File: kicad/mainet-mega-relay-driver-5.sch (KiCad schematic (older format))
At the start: 8 parts, among them J34 Screw_Terminal_01x03, K5 SANYOU_SRD_Form_C, Q5 2N3904, U6 4N37

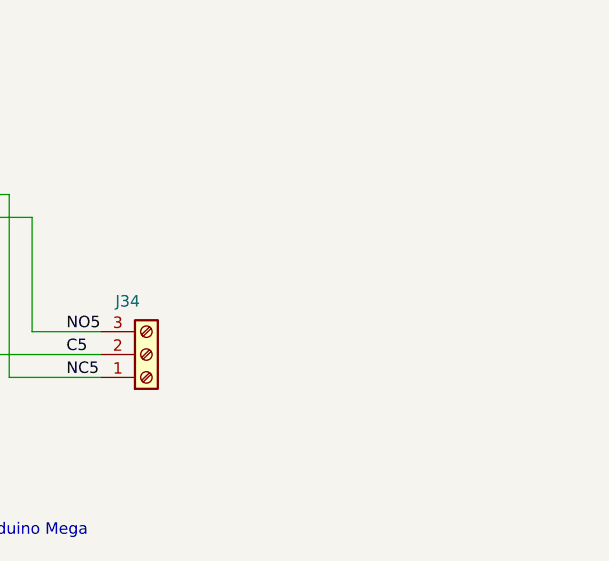
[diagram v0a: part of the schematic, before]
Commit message: KICAD: Actualizar esquemáticos
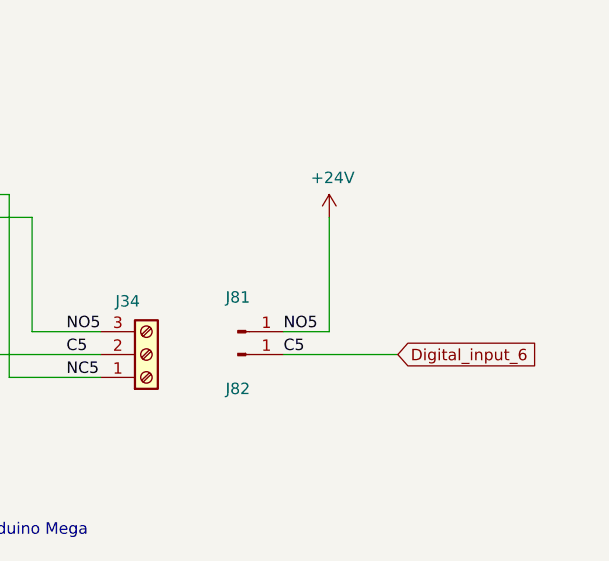
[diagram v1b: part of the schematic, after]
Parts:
- added J81, J82: Conn_01x01_Male, symbol Connector:Conn_01x01_Male
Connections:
- net C5 renamed Digital_input_6
- net Digital_input_6: now also J82.1 (Pin_1)
- net NO5 renamed +24V
- net +24V: now also J81.1 (Pin_1)
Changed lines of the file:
@@
 Sheet 11 21
 Title "Mainet-mega -- "
-Date "2021-04-06"
+Date "2021-04-07"
 Rev "1.0"
 Comp "Tovenca"
@@
 Text Notes 3650 4250 0    50   ~ 0
 D17-jogForwardControl
+$Comp
+L Connector:Conn_01x01_Male J?
+U 1 1 60704034
+P 8700 3600
+AR Path="/5FC25793/5FD90A95/60704034" Ref="J?"  Part="1"
+AR Path="/5FC25793/5FD919F3/60704034" Ref="J81"  Part="1"
+F 0 "J81" H 8700 3750 50  0000 C CNN
+F 1 "Conn_01x01_Male" H 8808 3690 50  0001 C CNN
+F 2 "" H 8700 3600 50  0001 C CNN
+F 3 "~" H 8700 3600 50  0001 C CNN
+	1    8700 3600
+	1    0    0    -1
+$EndComp
+$Comp
+L Connector:Conn_01x01_Male J?
+U 1 1 6070403A
+P 8700 3700
+AR Path="/5FC25793/5FD90A95/6070403A" Ref="J?"  Part="1"
+AR Path="/5FC25793/5FD919F3/6070403A" Ref="J82"  Part="1"
+F 0 "J82" H 8700 3550 50  0000 C CNN
+F 1 "Conn_01x01_Male" H 8808 3790 50  0001 C CNN
+F 2 "" H 8700 3700 50  0001 C CNN
+F 3 "~" H 8700 3700 50  0001 C CNN
+	1    8700 3700
+	1    0    0    -1
+$EndComp
+$Comp
+L power:+24V #PWR?
+U 1 1 60704040
+P 9100 3100
+AR Path="/5FC25793/5FD90A95/60704040" Ref="#PWR?"  Part="1"
+AR Path="/5FC25793/5FD919F3/60704040" Ref="#PWR044"  Part="1"
+F 0 "#PWR044" H 9100 2950 50  0001 C CNN
+F 1 "+24V" H 9115 3273 50  0000 C CNN
+F 2 "" H 9100 3100 50  0001 C CNN
+F 3 "" H 9100 3100 50  0001 C CNN
+	1    9100 3100
+	1    0    0    -1
+$EndComp
+Wire Wire Line
+	9100 3100 9100 3600
+Wire Wire Line
+	9100 3600 8900 3600
+Text Label 8900 3600 0    50   ~ 0
+NO5
+Text Label 8900 3700 0    50   ~ 0
+C5
+Wire Wire Line
+	8900 3700 9400 3700
+Text GLabel 9400 3700 2    50   Input ~ 0
+Digital_input_6
 $EndSCHEMATC

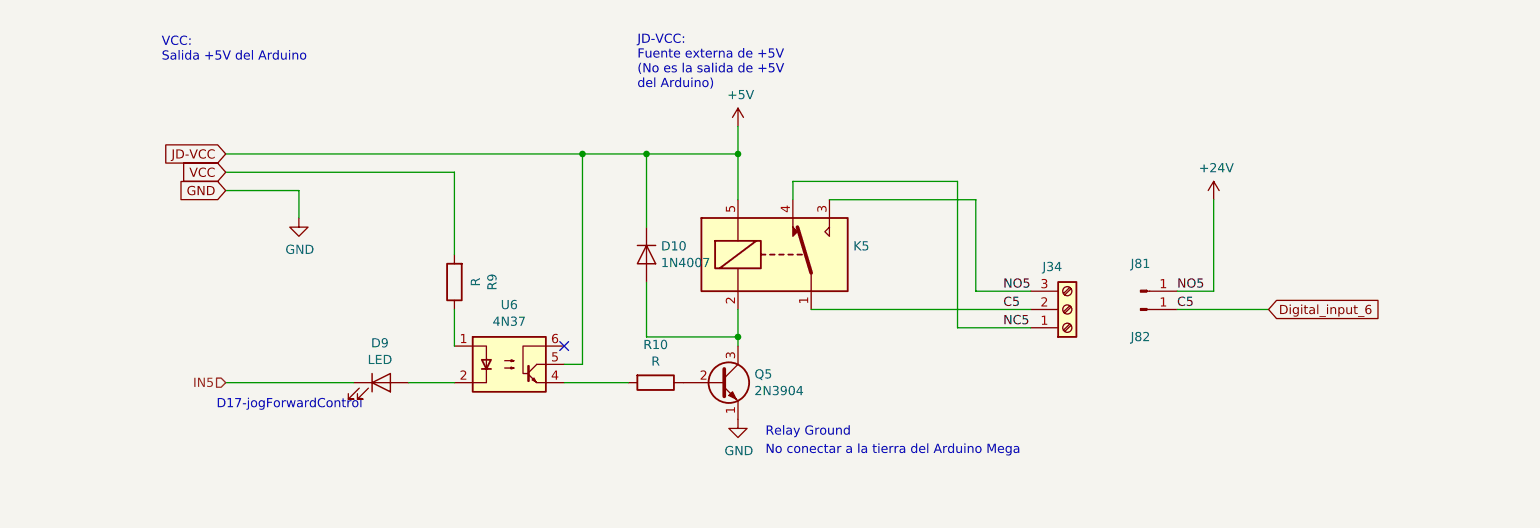
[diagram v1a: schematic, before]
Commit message: KICAD: Modificar esquemático
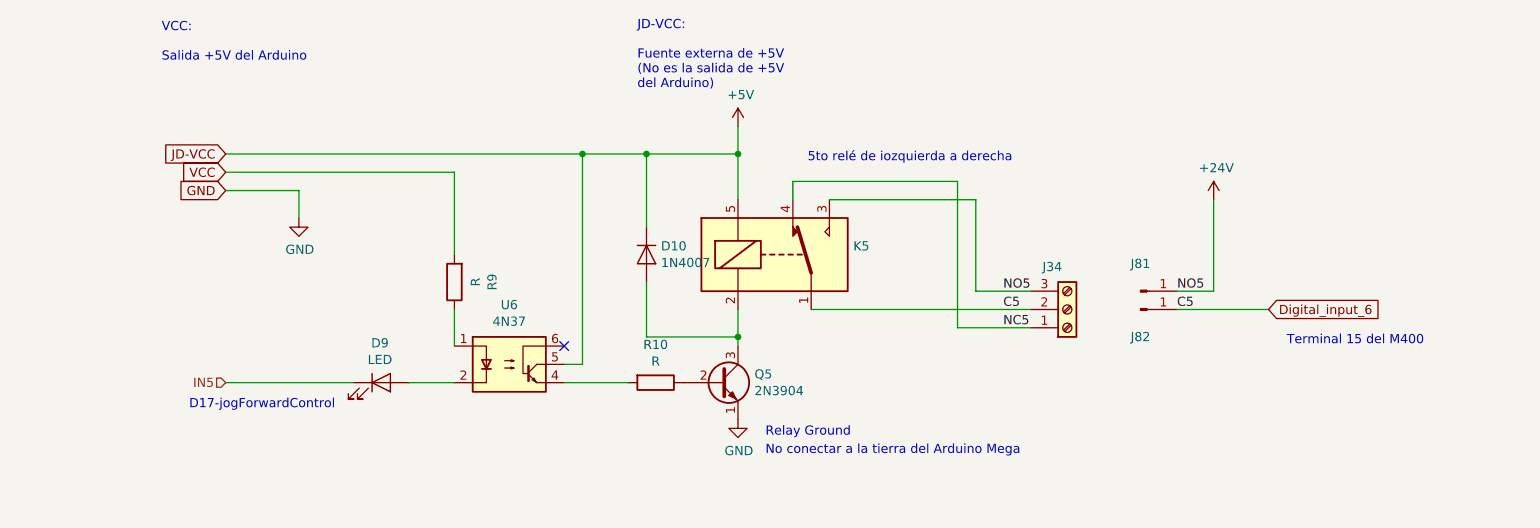
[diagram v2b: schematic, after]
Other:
- note added: "5to relé de iozquierda a derecha"
- note added: "JD-VCC:\n\nFuente externa de +5V\n(No es la salida de +5V \ndel Arduino)"
- note added: "Terminal 15 del M400"
- note added: "VCC:\n\nSalida +5V del Arduino"
- note removed: "JD-VCC:\nFuente externa de +5V\n(No es la salida de +5V \ndel Arduino)"
- note removed: "VCC:\nSalida +5V del Arduino"
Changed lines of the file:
@@
 EESchema Schematic File Version 4
+LIBS:mainet-mega-cache
 EELAYER 30 0
 EELAYER END
@@
 VCC
 Text Notes 5950 2500 0    50   ~ 0
-JD-VCC:\nFuente externa de +5V\n(No es la salida de +5V \ndel Arduino)
+JD-VCC:\n\nFuente externa de +5V\n(No es la salida de +5V \ndel Arduino)
 Text Notes 3350 2350 0    50   ~ 0
-VCC:\nSalida +5V del Arduino
-Text Notes 3650 4250 0    50   ~ 0
+VCC:\n\nSalida +5V del Arduino
+Text Notes 3500 4250 0    50   ~ 0
 D17-jogForwardControl
 $Comp
@@
 Text GLabel 9400 3700 2    50   Input ~ 0
 Digital_input_6
+Text Notes 8000 2900 2    50   ~ 0
+5to relé de iozquierda a derecha
+Text Notes 10250 3900 2    50   ~ 0
+Terminal 15 del M400
 $EndSCHEMATC

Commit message: KICAD: Actualizar archivos del módulo de relés
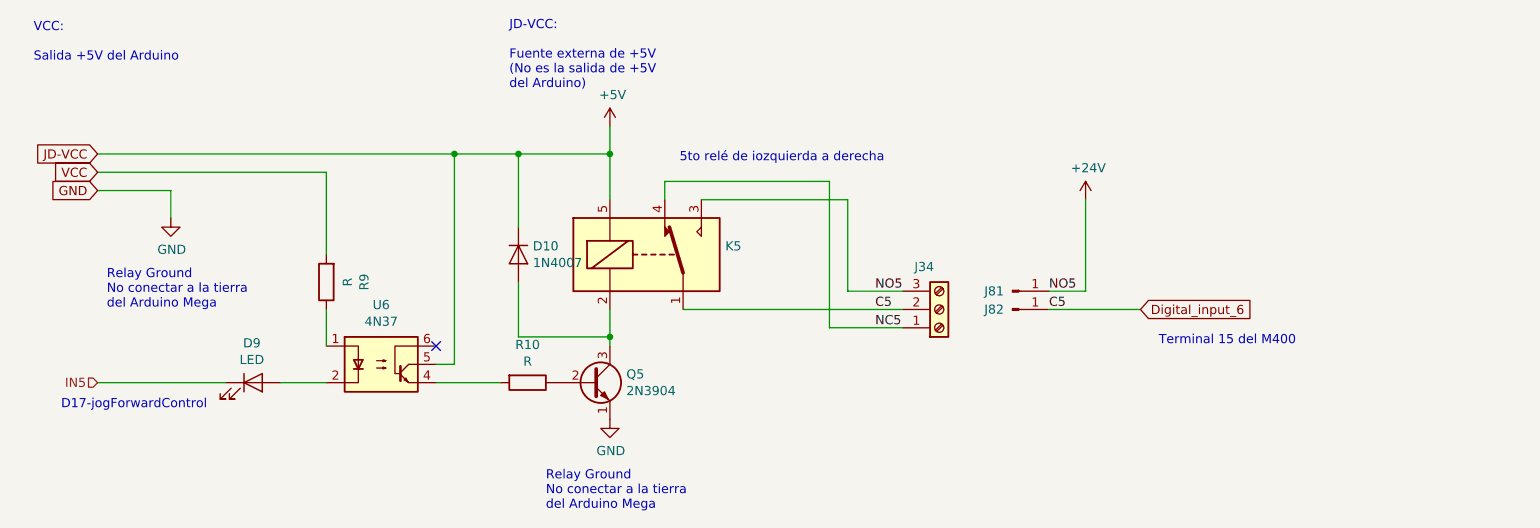
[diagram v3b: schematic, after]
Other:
- note added: "Relay Ground\nNo conectar a la tierra\ndel Arduino Mega\n"
- note removed: "No conectar a la tierra del Arduino Mega\n"
- note removed: "Relay Ground\n"
- moved on the sheet: D10, D9, J34, J81, J82, K5, Q5, R10, R9, U6

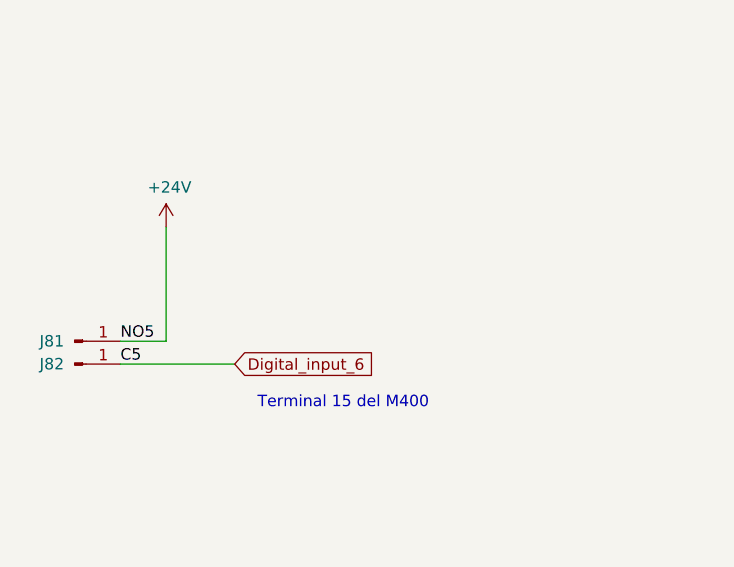
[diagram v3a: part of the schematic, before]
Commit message: KICAD: Agregar cambios esquemáticos
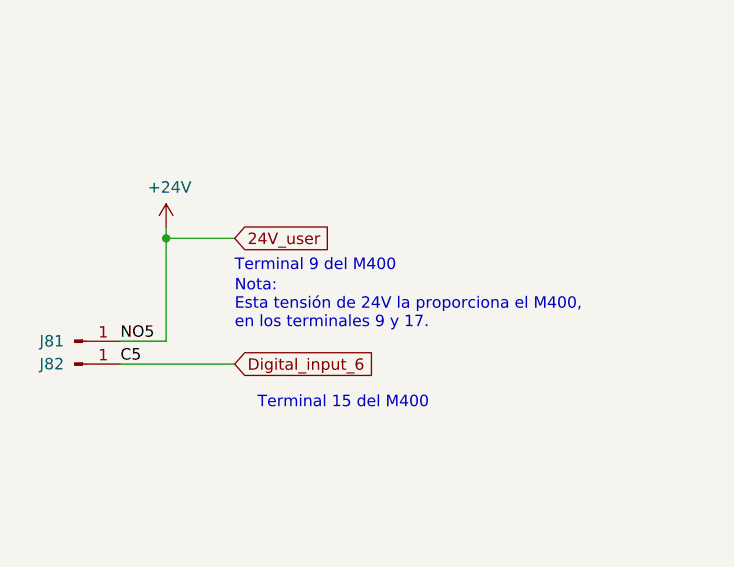
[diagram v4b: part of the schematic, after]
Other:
- note added: "Nota:\nEsta tensión de 24V la proporciona el M400, \nen los terminales 9 y 17."
- note added: "Terminal 9 del M400"
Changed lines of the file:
@@
 Sheet 11 22
 Title "Mainet-mega -- "
-Date "2021-04-07"
+Date "2021-06-18"
 Rev "1.0"
 Comp "Tovenca"
@@
 $EndComp
 Wire Wire Line
-	8400 3100 8400 3600
+	8400 3100 8400 3150
 Wire Wire Line
 	8400 3600 8200 3600
@@
 Text Notes 3050 3700 0    50   ~ 0
 Relay Ground\nNo conectar a la tierra\ndel Arduino Mega\n
+Text GLabel 8700 3150 2    50   Input ~ 0
+24V_user
+Wire Wire Line
+	8400 3150 8700 3150
+Text Notes 8700 3300 0    50   ~ 0
+Terminal 9 del M400
+Text Notes 8700 3550 0    50   ~ 0
+Nota:\nEsta tensión de 24V la proporciona el M400, \nen los terminales 9 y 17.
+Connection ~ 8400 3150
+Wire Wire Line
+	8400 3150 8400 3600
 $EndSCHEMATC
